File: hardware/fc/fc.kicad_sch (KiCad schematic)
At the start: 40 parts, among them SW1 Push, U12 RP2354A, X1 ABM8-272-T3

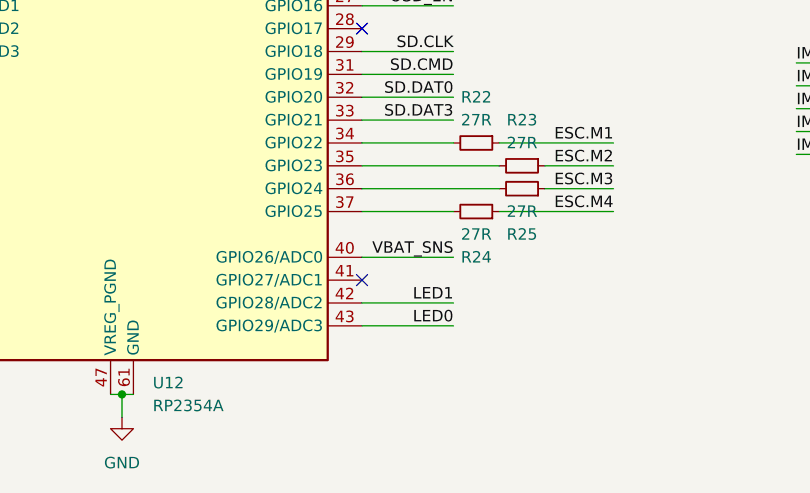
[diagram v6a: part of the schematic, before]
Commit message: fc: add rbleed, swap comparator, clamp video to vref
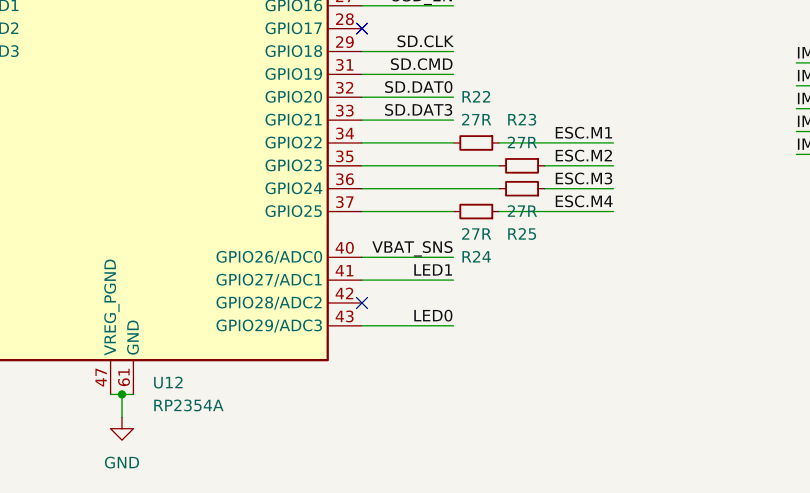
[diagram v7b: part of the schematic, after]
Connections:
- net LED1: now also U12.41 (GPIO27/ADC1); no longer U12.42 (GPIO28/ADC2)
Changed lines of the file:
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@@
-	)
-	(no_connect
-		(at 128.27 160.02)
 	)
 	(no_connect
@@
 	(no_connect
 		(at 128.27 132.08)
+	)
+	(no_connect
+		(at 128.27 162.56)
 	)
 	(no_connect
@@
 	(wire
 		(pts
-			(xy 138.43 162.56) (xy 128.27 162.56)
-		)
-		(stroke
-			(width 0)
-			(type default)
-		)
-	)
-	(wire
-		(pts
 			(xy 224.79 107.95) (xy 237.49 107.95)
 		)
@@
 		(pts
 			(xy 93.98 21.59) (xy 96.52 21.59)
+		)
+		(stroke
+			(width 0)
+			(type default)
+		)
+	)
+	(wire
+		(pts
+			(xy 138.43 160.02) (xy 128.27 160.02)
 		)
 		(stroke
@@
 		)
 	)
-	(label "LED1"
-		(at 138.43 162.56 180)
-		(effects
-			(font
-				(size 1.27 1.27)
-			)
-			(justify right bottom)
-		)
-	)
 	(label "ESC.M4"
 		(at 176.53 100.33 0)
@@
 		(effects
 			(font
+				(size 1.27 1.27)
+			)
+			(justify right bottom)
+		)
+	)
+	(label "LED1"
+		(at 138.43 160.02 180)
+		(effects
+			(font

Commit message: fc: move DC restoration/clamp to shared path
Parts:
- C32, C33: value 15p -> 15pF
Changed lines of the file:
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@@
 			)
 		)
-		(property "Value" "15p"
+		(property "Value" "15pF"
 			(at 62.23 134.62 90)
 			(show_name no)
@@
 			)
 		)
-		(property "Value" "15p"
+		(property "Value" "15pF"
 			(at 62.23 160.02 90)
 			(show_name no)
